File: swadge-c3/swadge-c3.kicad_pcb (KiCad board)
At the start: 2 copper layers, 73.7 x 89.4 mm, 65 parts, among them J1 USB_B_Micro, SW1 4-1437565-2, SW2 4-1437565-2, SW3 4-1437565-2, SW4 4-1437565-2, SW5 4-1437565-2, SW6 4-1437565-2, SW7 4-1437565-2, SW8 4-1437565-2, SW9 SW_SPDT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

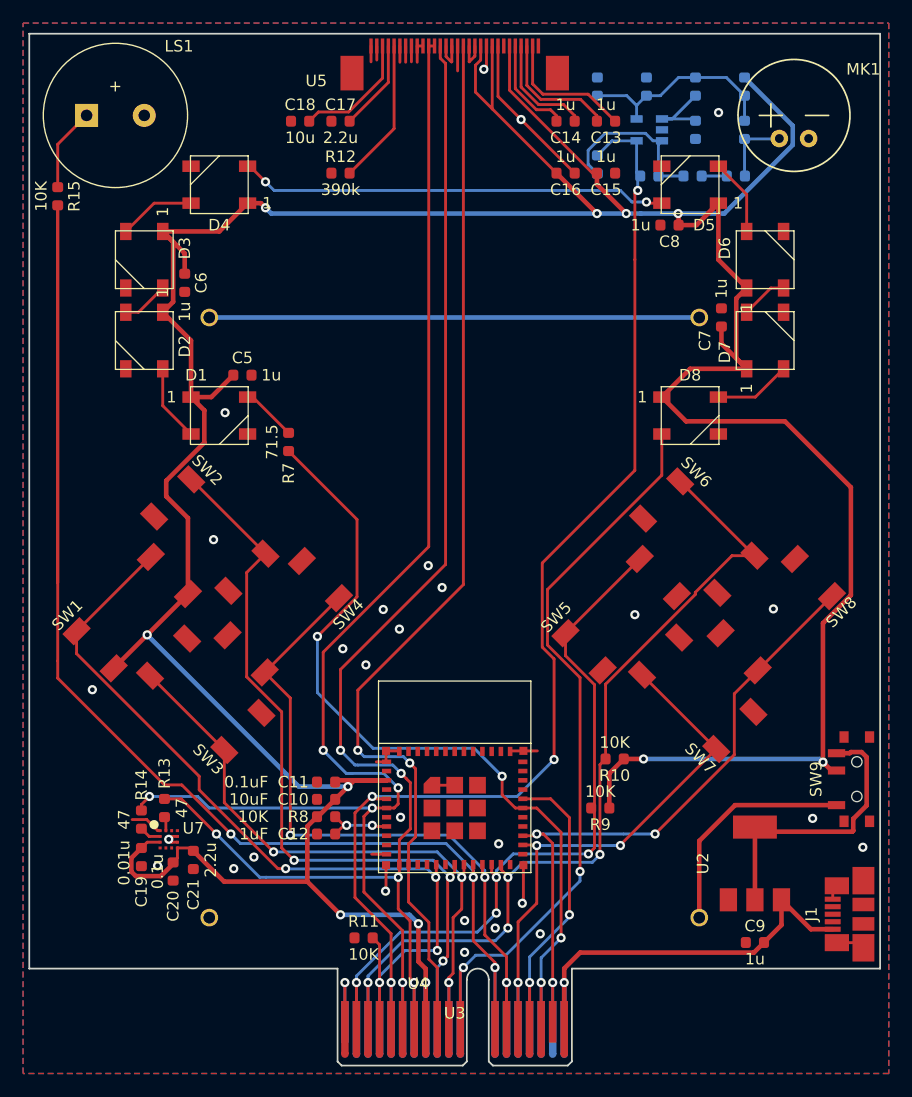
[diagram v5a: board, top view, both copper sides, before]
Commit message: Rounded corners
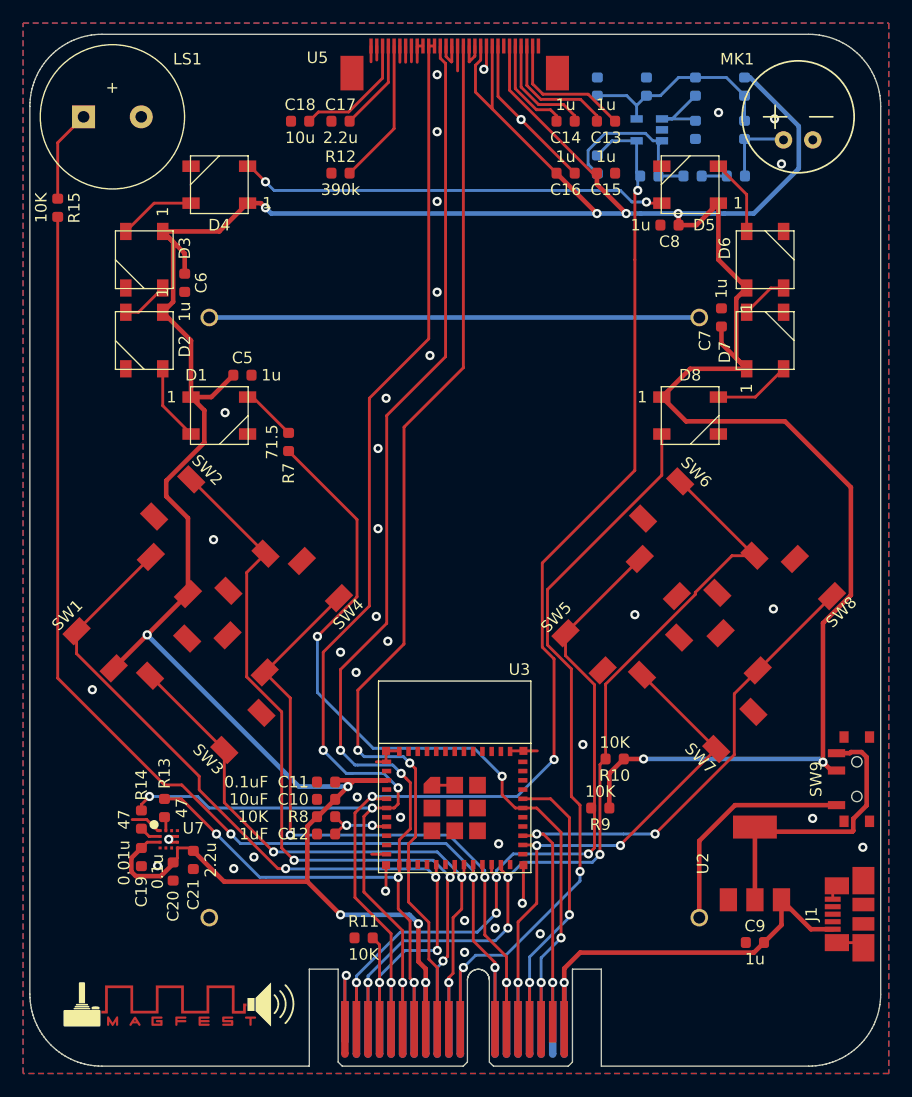
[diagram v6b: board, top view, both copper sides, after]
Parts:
- added svg2mod: G***, Swadge_Parts:MAGFEST_logo_centered_final, F.Cu at (121.5, 142.0)
- moved R15 1.00 mm to (111.0, 73.0)
- moved MK1 0.38 mm to (175.1, 65.1)
- moved LS1 0.29 mm to (115.7, 65.1)
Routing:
- net IO6_BZR: track 137.3 -> 103.5 mm
- net +3V3: track 356.1 -> 358.3 mm
- net GND: track 62.7 -> 64.0 mm, vias 29 -> 39
- net Net-(LS1-Pad1): track 7.25 -> 8.02 mm
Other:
- outline, holes or cut-outs redrawn

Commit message: Fix alignment
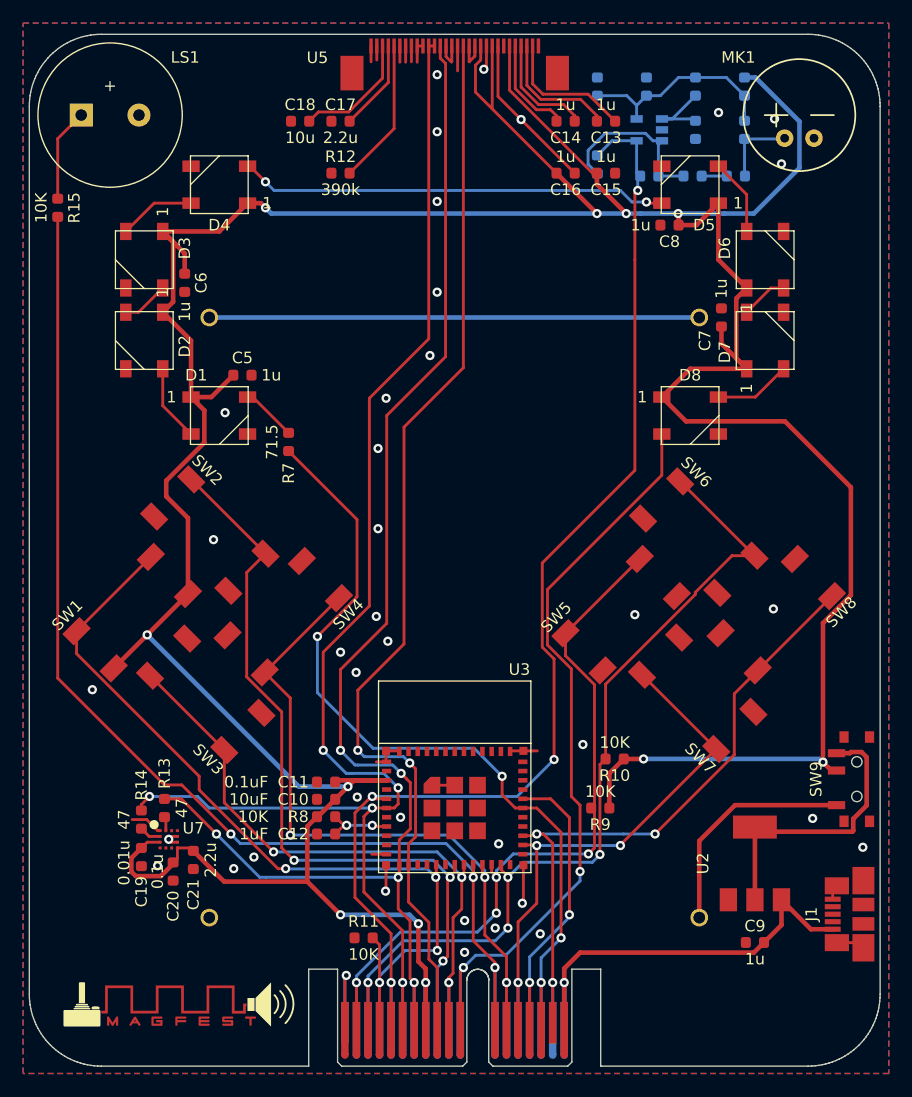
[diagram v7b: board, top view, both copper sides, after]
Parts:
- moved LS1 0.25 mm to (115.5, 65.0)
- moved MK1 0.18 mm to (175.2, 65.0)
- moved U4 0.08 mm to (135.9, 143.6)

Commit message: Added art, renders, exported schematic
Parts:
- removed svg2mod: G***, Swadge_Parts:MAGFEST_logo_centered_final
- added Ref**: Val**, swadge-c3-art:label, F.Cu at (170.1, 141.8)
- added Ref**: Val**, swadge-c3-art:swadges, F.Cu at (145.4, 102.8)
- added Ref**: Val**, swadge-c3-art:mag-logo-metal, F.Cu at (120.8, 140.8)
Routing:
- net RX: track 73.5 -> 70.6 mm
- net IO3_SDA: track 122.8 -> 124.5 mm
- net IO2_MIC: track 105.9 -> 106.7 mm
- net IO7_SW4: track 61.7 -> 61.5 mm, vias 3 -> 5
- net GND: vias 39 -> 42
